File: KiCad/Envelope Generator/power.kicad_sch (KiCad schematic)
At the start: 3 parts, among them U1 TL074, U2 TL074, U3 TL074

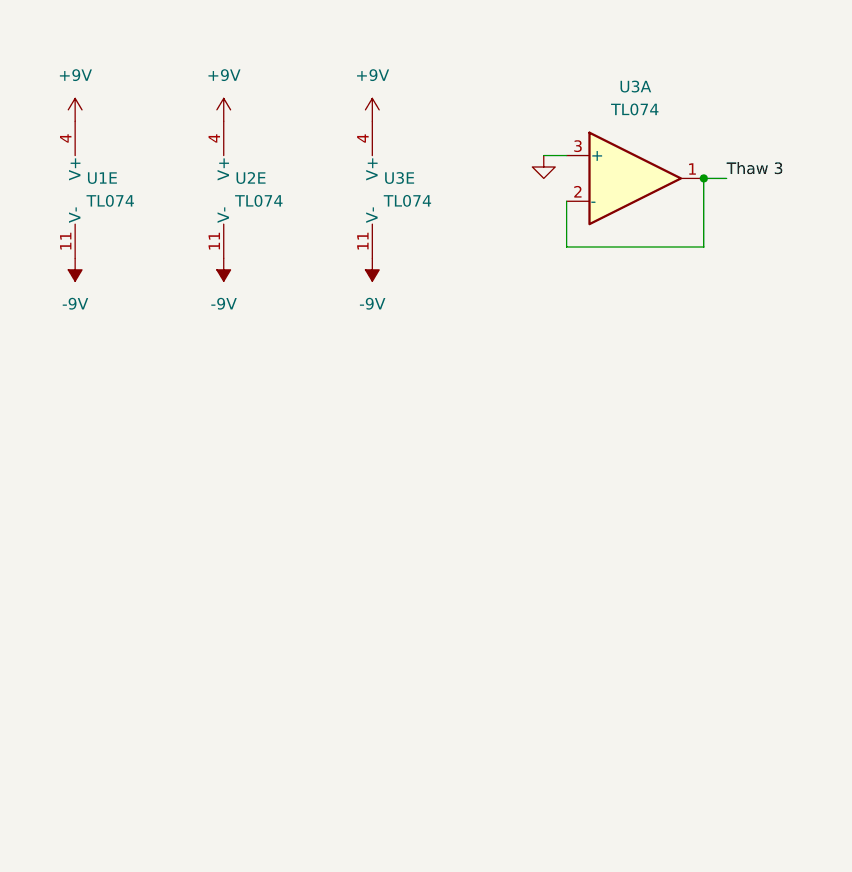
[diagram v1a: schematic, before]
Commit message: finished separating into separate kicad projects
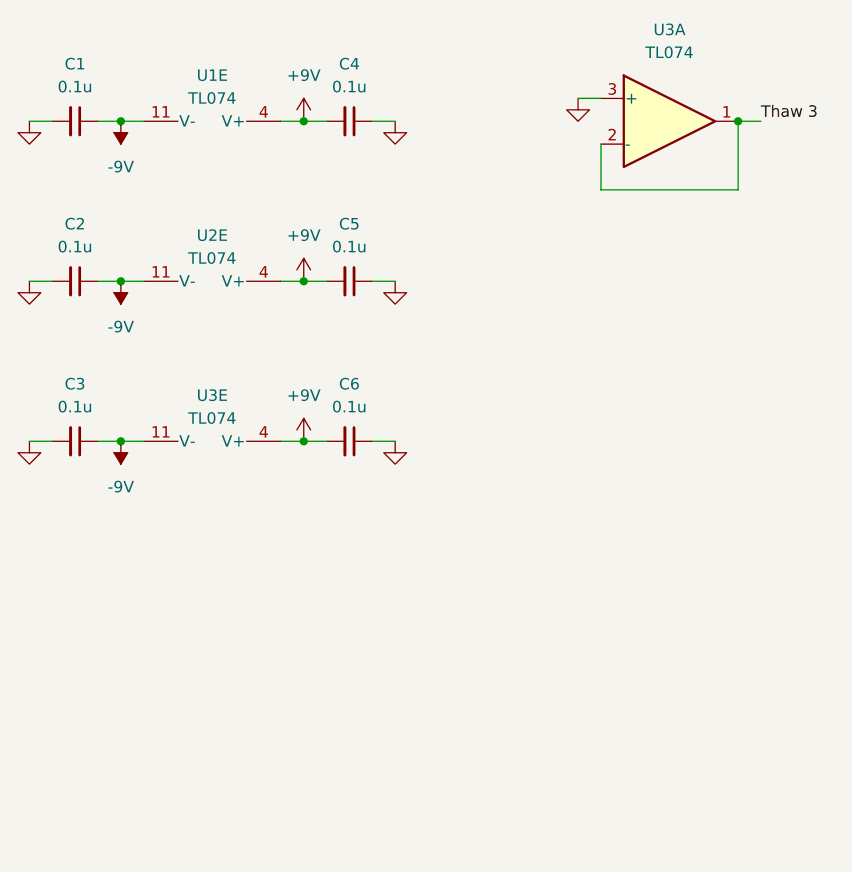
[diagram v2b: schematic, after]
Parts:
- added C1, C2, C3, C4, C5, C6: 0.1u, symbol Device:C_Small
- U1, U2, U3: footprint Package_DIP:DIP-14_W7.62mm -> (none)
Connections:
- net +9V: now also C4.2, C5.2, C6.2
- net -9V: now also C1.1, C2.1, C3.1
- net GND: now also C1.2, C2.2, C3.2, C4.1, C5.1, C6.1
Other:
- moved on the sheet: U3A

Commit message: added power indicator LEDs
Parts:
- added D10, D11: LED, symbol Device:LED
- added R10, R9: R_US, symbol Device:R_US
- renumbered C5 to C10, C6 to C11, C1 to C6, C2 to C7, C3 to C8, C4 to C9
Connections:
- net +9V: now also D10.2 (A)
- net -9V: now also R10.2
- net GND: now also D11.2 (A), R9.2
- new net: D10.1 (K), R9.1
- new net: D11.1 (K), R10.1

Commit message: updated footprints in envelope generator
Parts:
- C10, C11, C6, C7, C8, C9: footprint (none) -> Capacitor_SMD:C_0805_2012Metric
- D10, D11: footprint (none) -> LED_THT:LED_D5.0mm
- R10, R9: footprint (none) -> Resistor_SMD:R_0805_2012Metric
- U1, U2, U3: footprint (none) -> Package_DIP:DIP-14_W7.62mm
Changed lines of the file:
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@@
 			)
 		)
-		(property "Footprint" ""
+		(property "Footprint" "Package_DIP:DIP-14_W7.62mm"
 			(at 43.18 67.31 0)
 			(hide yes)
@@
 			)
 		)
-		(property "Footprint" ""
+		(property "Footprint" "Resistor_SMD:R_0805_2012Metric"
 			(at 38.354 87.884 90)
 			(hide yes)
@@
 			)
 		)
-		(property "Footprint" ""
+		(property "Footprint" "Package_DIP:DIP-14_W7.62mm"
 			(at 43.18 49.53 0)
 			(hide yes)
@@
 			)
 		)
-		(property "Footprint" ""
+		(property "Footprint" "Package_DIP:DIP-14_W7.62mm"
 			(at 43.18 31.75 0)
 			(hide yes)
@@
 			)
 		)
-		(property "Footprint" ""
+		(property "Footprint" "LED_THT:LED_D5.0mm"
 			(at 26.67 88.9 0)
 			(hide yes)
@@
 			)
 		)
-		(property "Footprint" ""
+		(property "Footprint" "Capacitor_SMD:C_0805_2012Metric"
 			(at 25.4 66.04 0)
 			(hide yes)
@@
 			)
 		)
-		(property "Footprint" ""
+		(property "Footprint" "Capacitor_SMD:C_0805_2012Metric"
 			(at 55.88 66.04 0)
 			(hide yes)
@@
 			)
 		)
-		(property "Footprint" ""
+		(property "Footprint" "Capacitor_SMD:C_0805_2012Metric"
 			(at 55.88 48.26 0)
 			(hide yes)
@@
 			)
 		)
-		(property "Footprint" ""
+		(property "Footprint" "Capacitor_SMD:C_0805_2012Metric"
 			(at 55.88 30.48 0)
 			(hide yes)
@@
 			)
 		)
-		(property "Footprint" ""
+		(property "Footprint" "Resistor_SMD:R_0805_2012Metric"
 			(at 38.354 104.394 90)
 			(hide yes)
@@
 			)
 		)
-		(property "Footprint" ""
+		(property "Footprint" "LED_THT:LED_D5.0mm"
 			(at 26.67 105.41 0)
 			(hide yes)
@@
 			)
 		)
-		(property "Footprint" ""
+		(property "Footprint" "Capacitor_SMD:C_0805_2012Metric"
 			(at 25.4 30.48 0)
 			(hide yes)
@@
 			)
 		)
-		(property "Footprint" ""
+		(property "Footprint" "Capacitor_SMD:C_0805_2012Metric"
 			(at 25.4 48.26 0)
 			(hide yes)

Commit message: envelope generator pcb layout done
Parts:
- R10, R9: value R_US -> 1k
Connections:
- net -9V: now also D11.2 (A); no longer R10.2
- net GND: now also R10.2, U3.5 (+); no longer D11.2 (A), U3.3 (+)
- net Thaw 3: now also U3.6 (-), U3.7; no longer U3.1, U3.2 (-)
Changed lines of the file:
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@@
 			)
 		)
-		(property "Value" "R_US"
+		(property "Value" "1k"
 			(at 38.1 85.09 90)
 			(show_name no)
@@
 	(symbol
 		(lib_id "power:GND")
-		(at 21.59 105.41 0)
+		(at 43.18 105.41 0)
 		(unit 1)
 		(body_style 1)
@@
 		(fields_autoplaced yes)
 		(property "Reference" "#PWR026"
-			(at 21.59 111.76 0)
+			(at 43.18 111.76 0)
 			(hide yes)
 			(show_name no)
@@
 		)
 		(property "Value" "GND"
-			(at 21.59 110.49 0)
+			(at 43.18 110.49 0)
 			(hide yes)
 			(show_name no)
@@
 		)
 		(property "Footprint" ""
-			(at 21.59 105.41 0)
-			(hide yes)
-			(show_name no)
-			(do_not_autoplace no)
-			(effects
-				(font
-					(size 1.27 1.27)
-				)
-			)
-		)
-		(property "Datasheet" ""
-			(at 21.59 105.41 0)
+			(at 43.18 105.41 0)
+			(hide yes)
+			(show_name no)
+			(do_not_autoplace no)
+			(effects
+				(font
+					(size 1.27 1.27)
+				)
+			)
+		)
+		(property "Datasheet" ""
+			(at 43.18 105.41 0)
 			(hide yes)
 			(show_name no)
@@
 		)
 		(property "Description" "Power symbol creates a global label with name \"GND\" , ground"
-			(at 21.59 105.41 0)
+			(at 43.18 105.41 0)
 			(hide yes)
 			(show_name no)
@@
 		(lib_id "Amplifier_Operational:TL074")
 		(at 91.44 30.48 0)
-		(unit 1)
+		(unit 2)
 		(body_style 1)
 		(exclude_from_sim no)
@@
 				(path "/3fd2dffe-1f54-47ff-9fe6-6fb87d577d3b"
 					(reference "U3")
-					(unit 1)
+					(unit 2)
 				)
 			)
@@
 			)
 		)
-		(property "Value" "R_US"
+		(property "Value" "1k"
 			(at 38.1 101.6 90)
 			(show_name no)
@@
 	(symbol
 		(lib_id "power:-9V")
-		(at 43.18 105.41 180)
+		(at 21.59 105.41 180)
 		(unit 1)
 		(body_style 1)
@@
 		(fields_autoplaced yes)
 		(property "Reference" "#PWR031"
-			(at 43.18 101.6 0)
+			(at 21.59 101.6 0)
 			(hide yes)
 			(show_name no)
@@
 		)
 		(property "Value" "-9V"
-			(at 43.18 110.49 0)
+			(at 21.59 110.49 0)
 			(show_name no)
 			(do_not_autoplace no)
@@
 		)
 		(property "Footprint" ""
-			(at 43.18 105.41 0)
-			(hide yes)
-			(show_name no)
-			(do_not_autoplace no)
-			(effects
-				(font
-					(size 1.27 1.27)
-				)
-			)
-		)
-		(property "Datasheet" ""
-			(at 43.18 105.41 0)
+			(at 21.59 105.41 0)
+			(hide yes)
+			(show_name no)
+			(do_not_autoplace no)
+			(effects
+				(font
+					(size 1.27 1.27)
+				)
+			)
+		)
+		(property "Datasheet" ""
+			(at 21.59 105.41 0)
 			(hide yes)
 			(show_name no)
@@
 		)
 		(property "Description" "Power symbol creates a global label with name \"-9V\""
-			(at 43.18 105.41 0)
-			(hide yes)
-			(show_name no)
+			(at 21.59 105.41 0)
+			(hide yes)
+			(show_name no)

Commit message: preparation to merge project back into one board
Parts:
- C10, C11, C6, C7, C8, C9, R10, R9: KiLib_Generator (none) -> SMD_2terminal_chip_molded
- D10, D11: KiLib_Generator (none) -> LED/THT
- U1, U2, U3: KiLib_Generator (none) -> package/DIP/legacy
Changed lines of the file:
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@@
+			)
+		)
+		(property "KiLib_Generator" "package/DIP/legacy"
+			(at 40.64 68.58 0)
+			(hide yes)
+			(show_name no)
+			(do_not_autoplace no)
+			(effects
+				(font
+					(size 1.27 1.27)
+				)
+			)
+		)
+		(property "LCSC Part #" ""
+			(at 40.64 68.58 0)
+			(hide yes)
+			(show_name no)
+			(do_not_autoplace no)
+			(effects
+				(font
+					(size 1.27 1.27)
+				)
 			)
 		)
@@
 			)
 		)
+		(property "KiLib_Generator" "SMD_2terminal_chip_molded"
+			(at 38.1 88.9 0)
+			(hide yes)
+			(show_name no)
+			(do_not_autoplace no)
+			(effects
+				(font
+					(size 1.27 1.27)
+				)
+			)
+		)
 		(pin "1"
 		)
@@
 		)
 		(property "Description" "Quad Low-Noise JFET-Input Operational Amplifiers, DIP-14/SOIC-14"
+			(at 40.64 50.8 0)
+			(hide yes)
+			(show_name no)
+			(do_not_autoplace no)
+			(effects
+				(font
+					(size 1.27 1.27)
+				)
+			)
+		)
+		(property "KiLib_Generator" "package/DIP/legacy"
+			(at 40.64 50.8 0)
+			(hide yes)
+			(show_name no)
+			(do_not_autoplace no)
+			(effects
+				(font
+					(size 1.27 1.27)
+				)
+			)
+		)
+		(property "LCSC Part #" ""
 			(at 40.64 50.8 0)
 			(hide yes)
@@
 			)
 		)
+		(property "KiLib_Generator" "package/DIP/legacy"
+			(at 40.64 33.02 0)
+			(hide yes)
+			(show_name no)
+			(do_not_autoplace no)
+			(effects
+				(font
+					(size 1.27 1.27)
+				)
+			)
+		)
+		(property "LCSC Part #" ""
+			(at 40.64 33.02 0)
+			(hide yes)
+			(show_name no)
+			(do_not_autoplace no)
+			(effects
+				(font
+					(size 1.27 1.27)
+				)
+			)
+		)
 		(pin "1"
 		)
@@
 			)
 		)
+		(property "KiLib_Generator" "package/DIP/legacy"
+			(at 91.44 30.48 0)
+			(hide yes)
+			(show_name no)
+			(do_not_autoplace no)
+			(effects
+				(font
+					(size 1.27 1.27)
+				)
+			)
+		)
 		(pin "10"
 		)
@@
 			)
 		)
+		(property "KiLib_Generator" "LED/THT"
+			(at 26.67 88.9 0)
+			(hide yes)
+			(show_name no)
+			(do_not_autoplace no)
+			(effects
+				(font
+					(size 1.27 1.27)
+				)
+			)
+		)
 		(pin "2"
 		)
@@
 			)
 		)
+		(property "KiLib_Generator" "SMD_2terminal_chip_molded"
+			(at 25.4 66.04 0)
+			(hide yes)
+			(show_name no)
+			(do_not_autoplace no)
+			(effects
+				(font
+					(size 1.27 1.27)
+				)
+			)
+		)
 		(pin "1"
 		)
@@
 			)
 		)
+		(property "KiLib_Generator" "SMD_2terminal_chip_molded"
+			(at 55.88 66.04 0)
+			(hide yes)
+			(show_name no)
+			(do_not_autoplace no)
+			(effects
+				(font
+					(size 1.27 1.27)
+				)
+			)
+		)
 		(pin "1"
 		)
@@
 			)
 		)
+		(property "KiLib_Generator" "SMD_2terminal_chip_molded"
+			(at 55.88 48.26 0)
+			(hide yes)
+			(show_name no)
+			(do_not_autoplace no)
+			(effects
+				(font
+					(size 1.27 1.27)
+				)
+			)
+		)
 		(pin "1"
 		)
@@
 			)
 		)
+		(property "KiLib_Generator" "SMD_2terminal_chip_molded"
+			(at 55.88 30.48 0)
+			(hide yes)
+			(show_name no)
+			(do_not_autoplace no)
+			(effects
+				(font
+					(size 1.27 1.27)
+				)
+			)
+		)
 		(pin "1"
 		)
@@
 			)
 		)
+		(property "KiLib_Generator" "SMD_2terminal_chip_molded"
+			(at 38.1 105.41 0)
+			(hide yes)
+			(show_name no)
+			(do_not_autoplace no)
+			(effects
+				(font
+					(size 1.27 1.27)
+				)
+			)
+		)
 		(pin "1"
 		)
@@
 			)
 		)
+		(property "KiLib_Generator" "LED/THT"
+			(at 26.67 105.41 0)
+			(hide yes)
+			(show_name no)
+			(do_not_autoplace no)
+			(effects
+				(font
+					(size 1.27 1.27)
+				)
+			)
+		)
 		(pin "2"
 		)
@@
 			)
 		)
+		(property "KiLib_Generator" "SMD_2terminal_chip_molded"
+			(at 25.4 30.48 0)
+			(hide yes)
+			(show_name no)
+			(do_not_autoplace no)
+			(effects
+				(font
+					(size 1.27 1.27)
+				)
+			)
+		)
 		(pin "1"
 		)
@@
 			(at 25.4 48.26 0)
 			(hide yes)
+			(show_name no)
+			(do_not_autoplace no)
+			(effects
+				(font
+					(size 1.27 1.27)
+				)
+			)
+		)
+		(property "KiLib_Generator" "SMD_2terminal_chip_molded"
+			(at 25.4 48.26 0)
+			(hide yes)
